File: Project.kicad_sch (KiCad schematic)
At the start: 3 parts, among them U1 ESP32-DEVKITC-32D

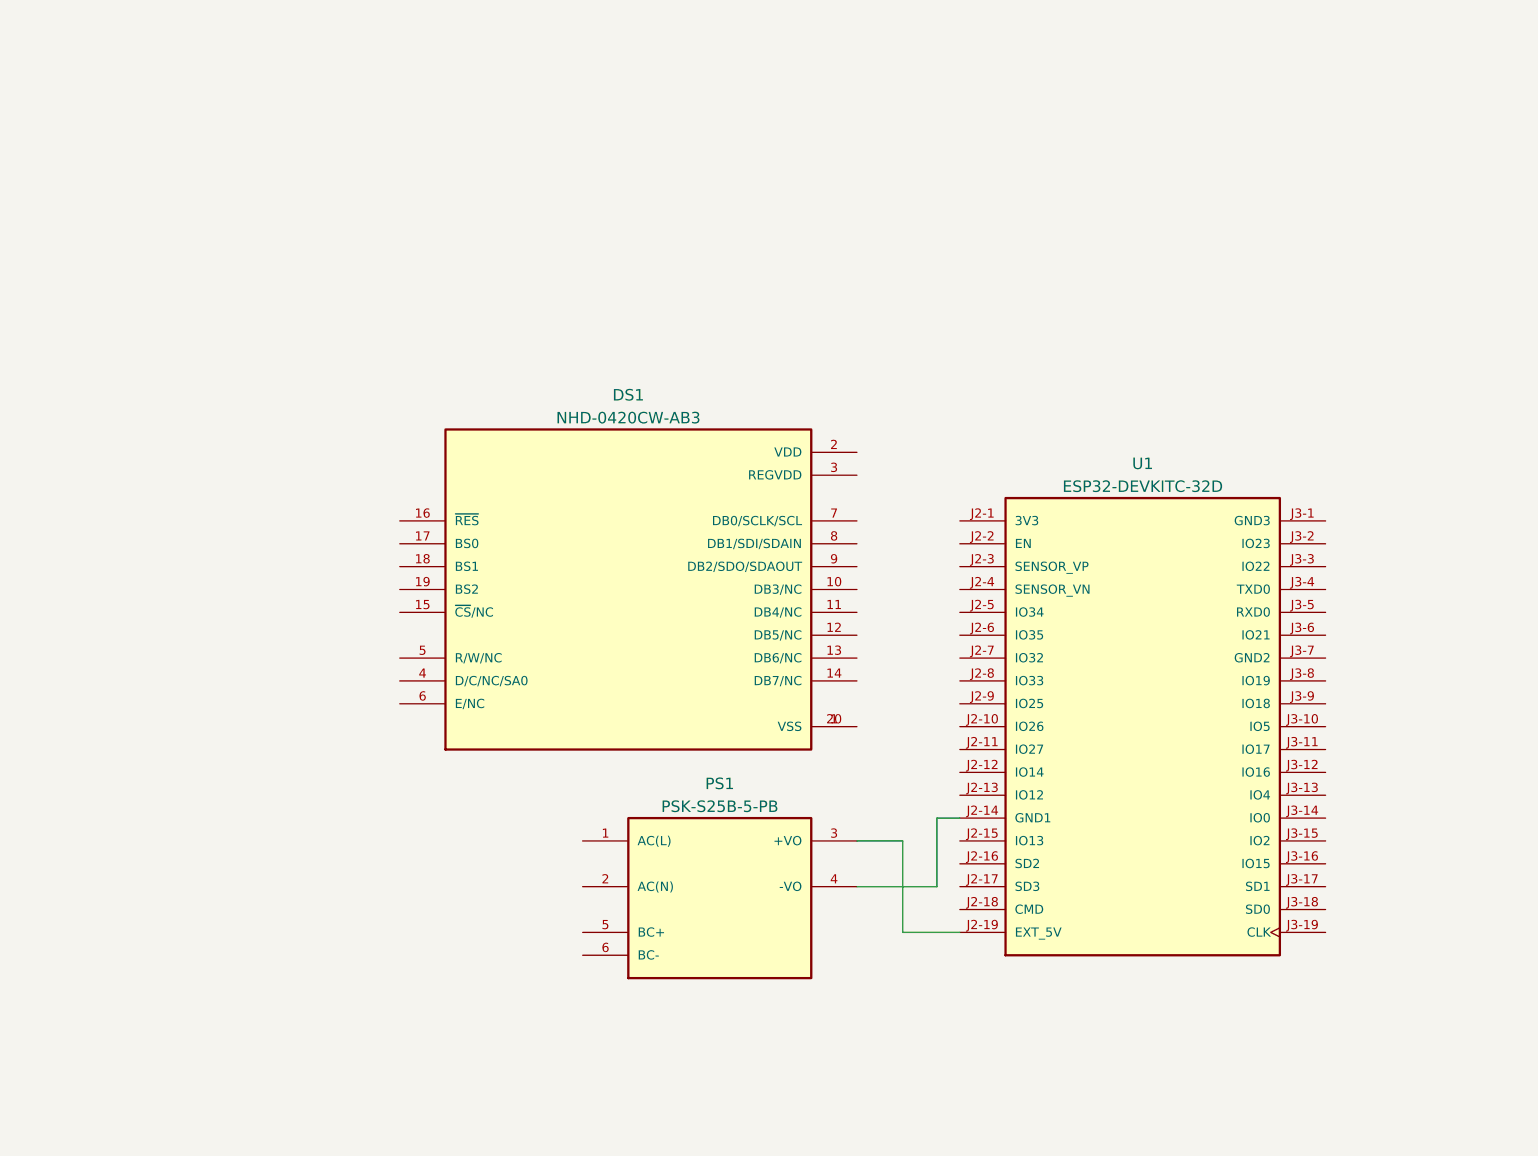
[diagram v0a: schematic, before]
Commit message: Add files via upload
The start of work with a correct layout and principles of design
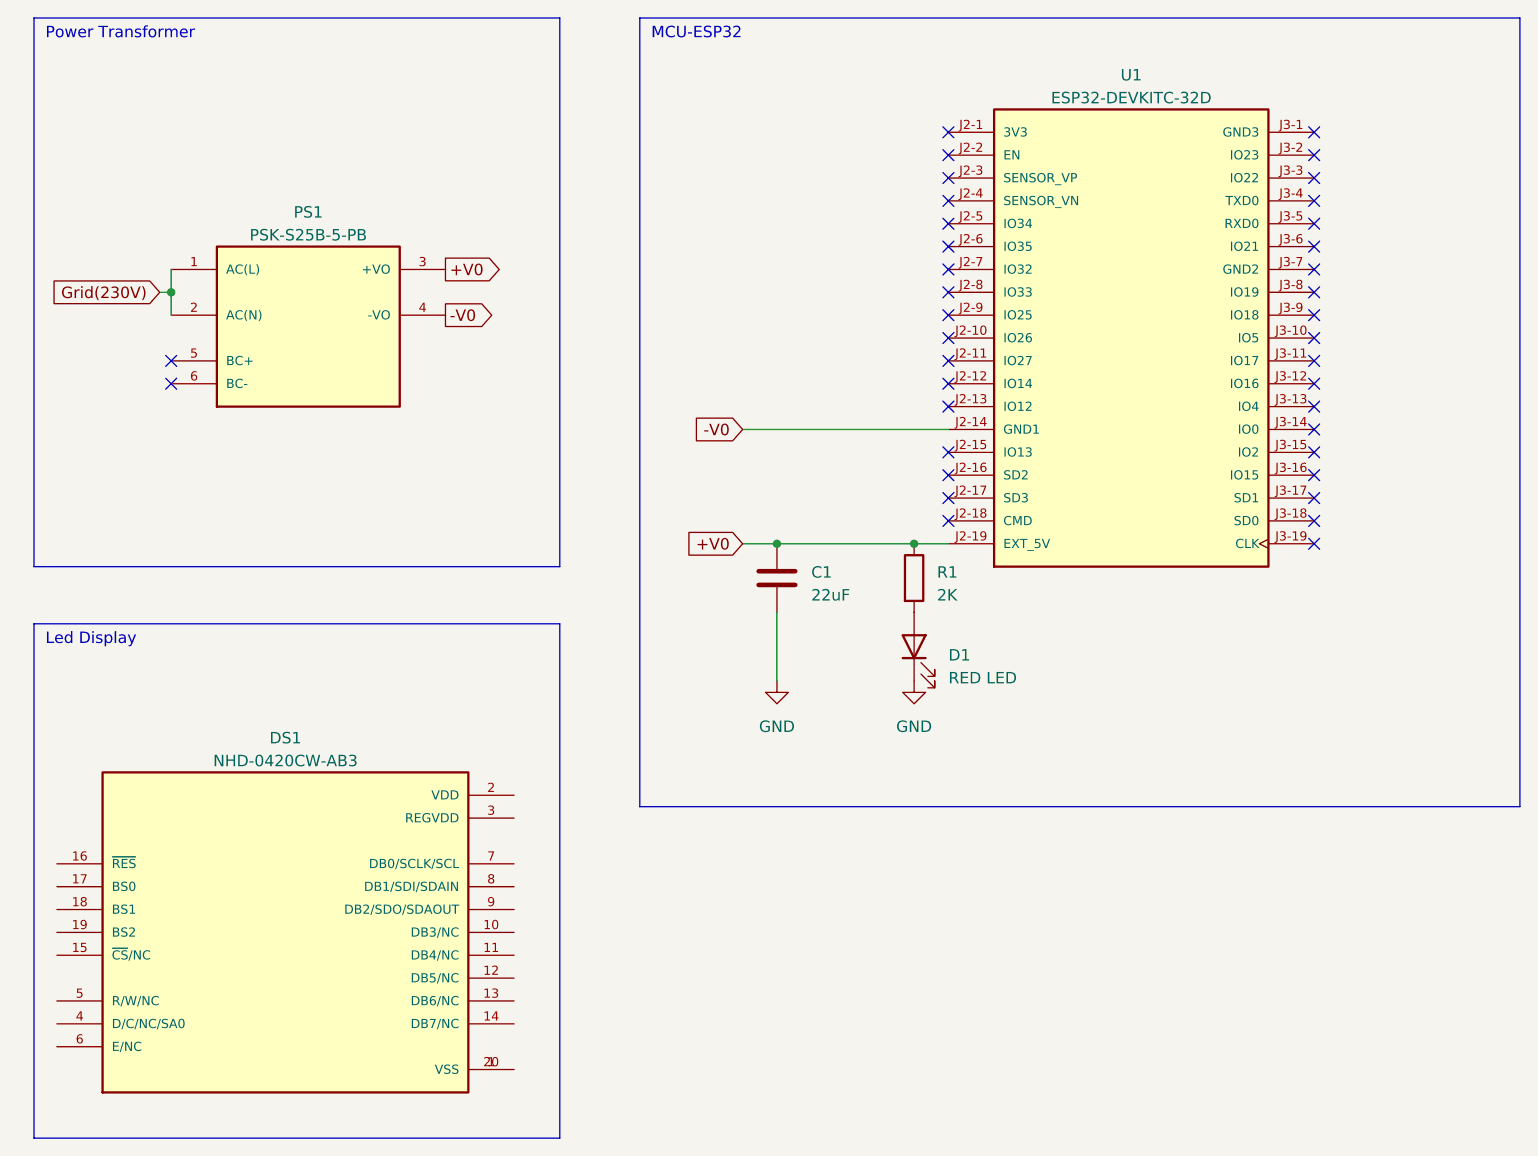
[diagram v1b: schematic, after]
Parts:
- added C1: 22uF, symbol Device:C
- added D1: RED LED, symbol Device:LED
- added R1: 2K, symbol Device:R
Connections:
- net -V0: now reaches PS1.4 (-VO), U1.J2-14 (GND1)
- net +V0: now reaches PS1.3 (+VO), U1.J2-19 (EXT_5V)
- net +V0: now also C1.1, R1.1
- net Grid(230V): now reaches PS1.1 (AC(L))
- net Grid(230V): now also PS1.2 (AC(N))
- new net: D1.2 (A), R1.2
- new net GND: C1.2, D1.1 (K)
- no-connect marks 0 -> 38
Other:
- note added: "Led Display"
- note added: "MCU-ESP32"
- note added: "Power Transformer"
- moved on the sheet: DS1, PS1

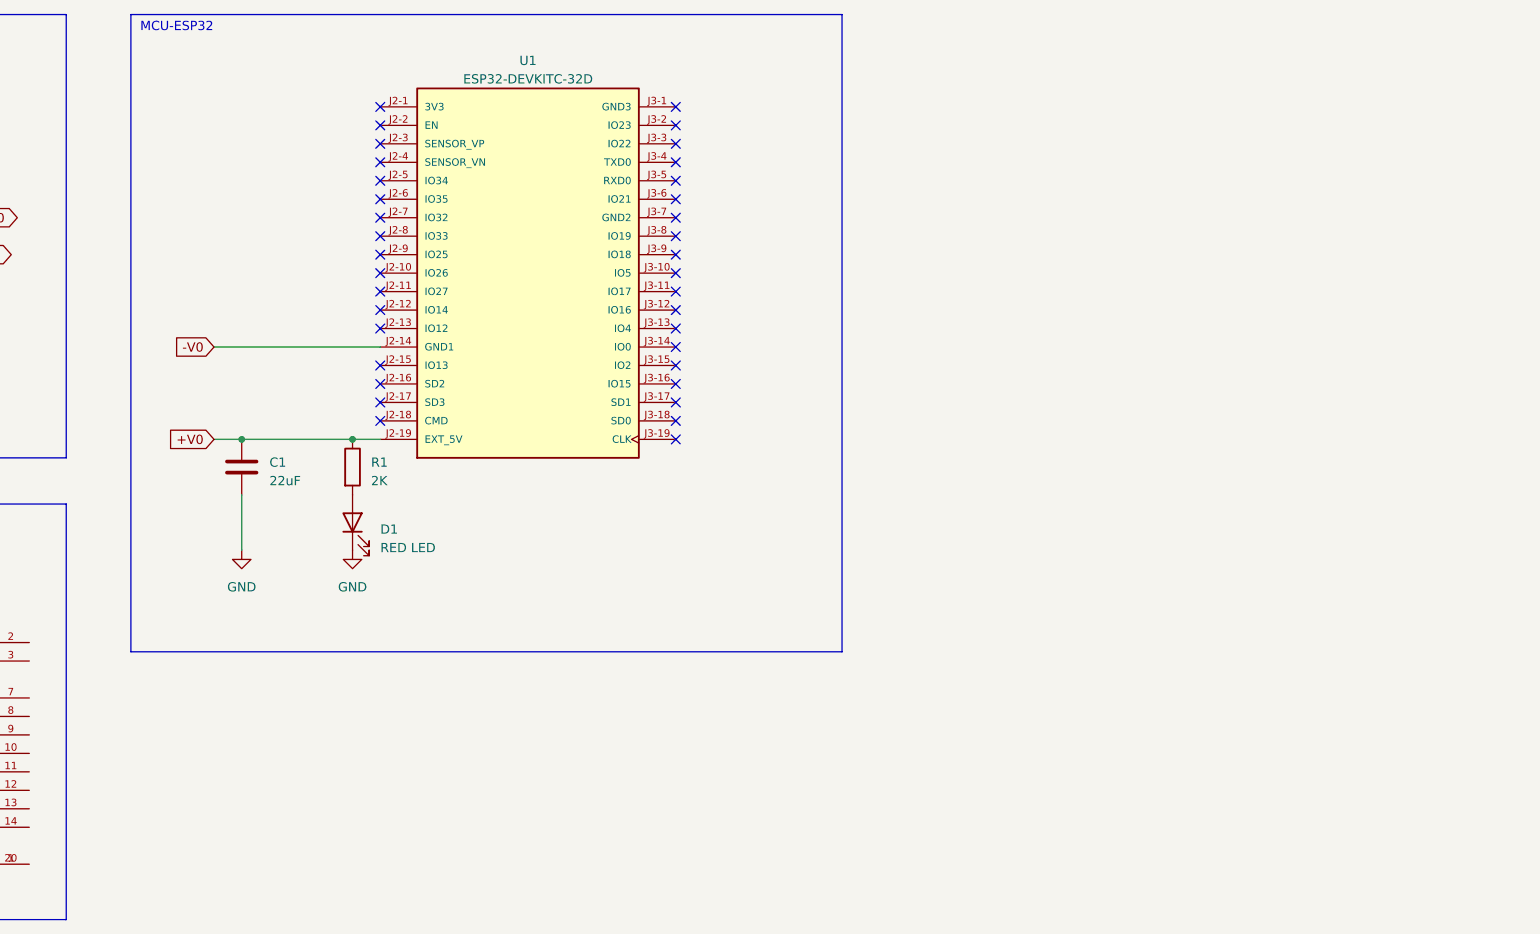
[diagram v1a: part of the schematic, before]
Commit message: Changed devboard to mcu
-Changed devboard to standalone mcu
-added 5v to 3.3v stabilizer
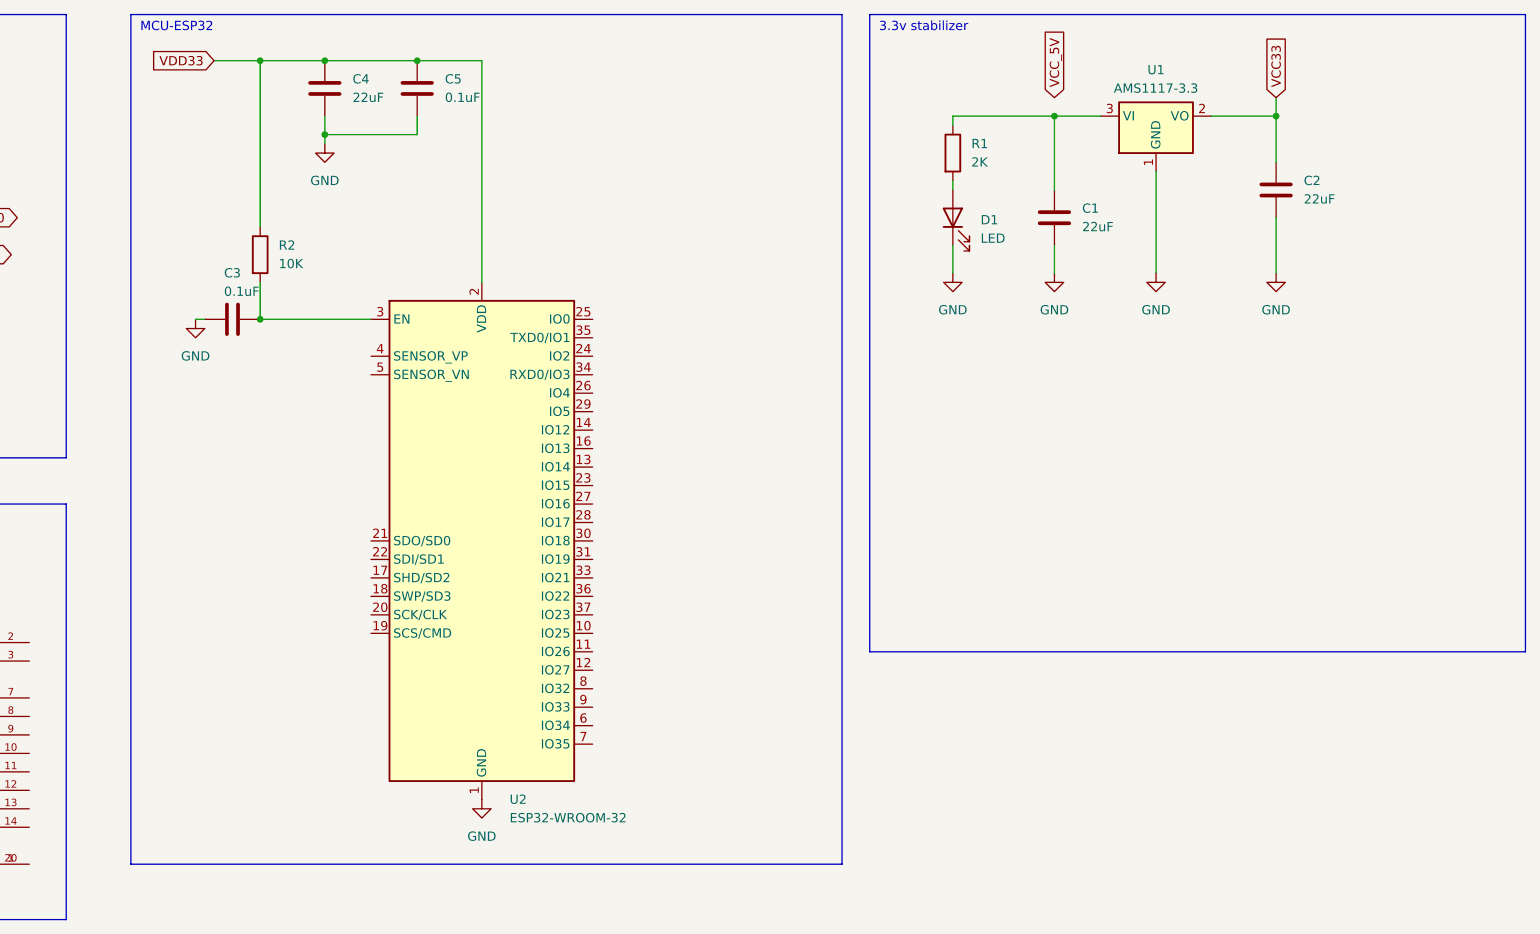
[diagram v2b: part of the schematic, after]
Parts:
- removed U1: ESP32-DEVKITC-32D, ESP32-DEVKITC-32D:MODULE_ESP32-DEVKITC-32D, symbol ESP32-DEVKITC-32D:ESP32-DEVKITC-32D
- added C2, C4: 22uF, symbol Device:C
- added C3, C5: 0.1uF, symbol Device:C
- added R2: 10K, symbol Device:R
- added U1: AMS1117-3.3, Package_TO_SOT_SMD:SOT-223-3_TabPin2, symbol Regulator_Linear:AMS1117-3.3
- added U2: ESP32-WROOM-32, RF_Module:ESP32-WROOM-32D, symbol RF_Module:ESP32-WROOM-32
- D1: value RED LED -> LED
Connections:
- net +V0: no longer C1.1, R1.1
- net GND: now also C2.2, C3.1, C4.2, C5.2, U1.1 (GND), U2.1 (GND), U2.15 (GND), U2.38 (GND), U2.39 (GND)
- new net: C1.1, R1.1, U1.3 (VI)
- new net: C3.2, R2.2, U2.3 (EN)
- new net VCC33: C2.1, U1.2 (VO)
- new net VDD33: C4.1, C5.1, R2.1, U2.2 (VDD)
- no-connect marks 38 -> 2
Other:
- note added: "3.3v stabilizer"
